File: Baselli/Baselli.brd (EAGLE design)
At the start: 54 x 54 mm, 81 parts, among them J1 FTDI-SER-6-PP, J2 DF12-ELLI-HEADER-TOP, J3 DF12-ELLI-RECEPTABLE-BOTTOM, J4 JTAG_PROG, Q1 8MHz NP, Q2 IRLML2244, SW1 A6H-2101, U1 STM32F051R, U4 LCMXO2-256HC-4SG32, X1 M-BOLT-2, X2 M-BOLT-2, X3 M-BOLT-2, X4 M-BOLT-2, X5 POE-TP-PD-BELFUSE-T568A, Y1 32.768 kHz

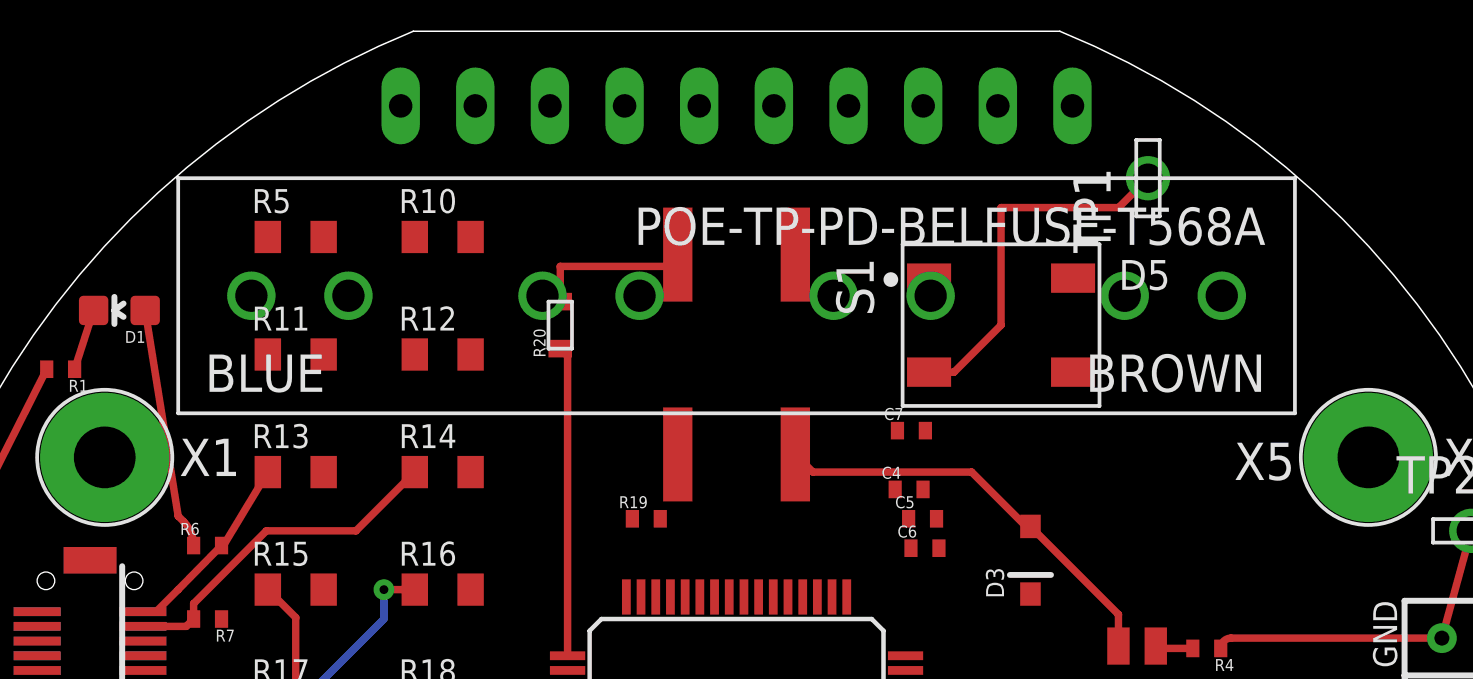
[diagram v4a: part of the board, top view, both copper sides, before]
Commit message: Remove excess punchdown connector from Baselli
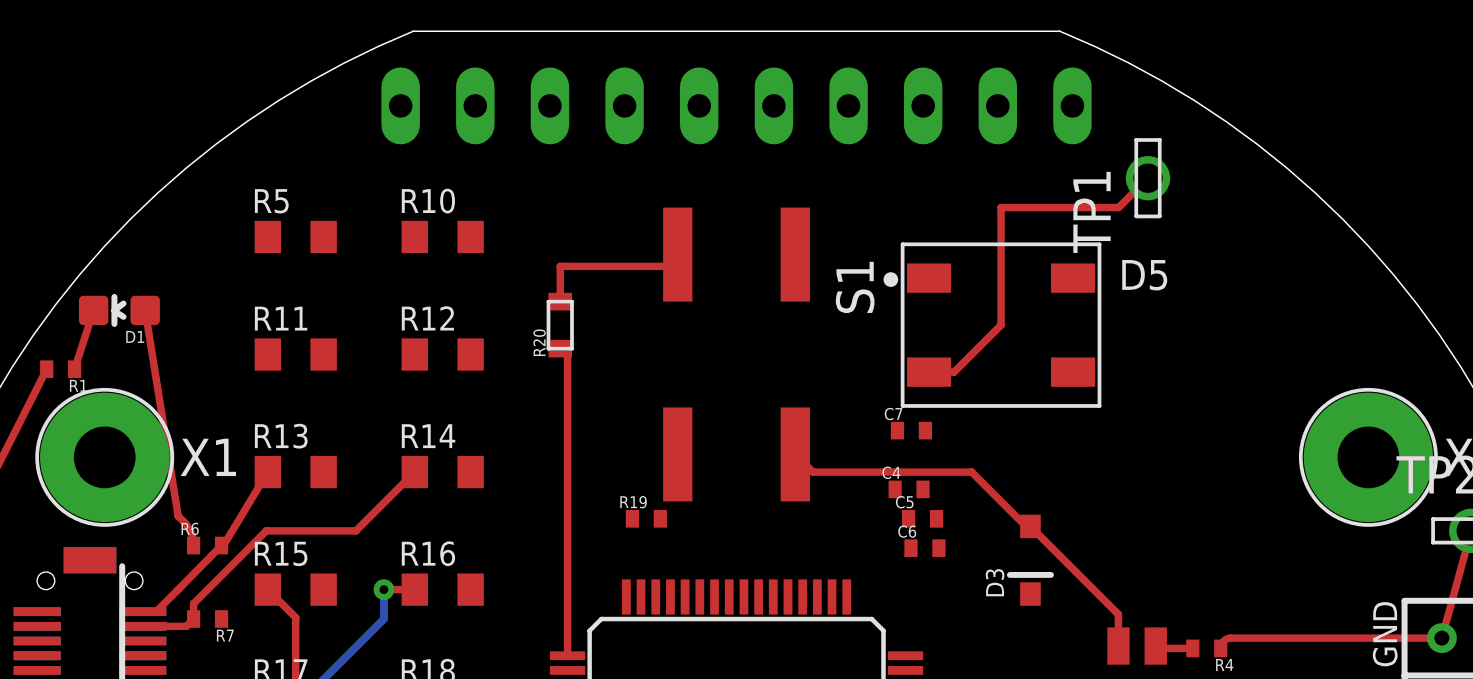
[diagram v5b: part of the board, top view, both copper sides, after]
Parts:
- removed X5: POE-TP-PD-BELFUSE-T568A, ELL-i-Connectors:BELFUSE-SS-51-PD-T568A
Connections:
- removed net POE+: X5.4, X5.5
- removed net POE-: X5.7, X5.8
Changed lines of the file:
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@@
 <layer number="17" name="Pads" color="2" fill="1" visible="yes" active="yes"/>
 <layer number="18" name="Vias" color="2" fill="1" visible="yes" active="yes"/>
-<layer number="19" name="Unrouted" color="6" fill="1" visible="yes" active="yes"/>
+<layer number="19" name="Unrouted" color="6" fill="1" visible="no" active="yes"/>
 <layer number="20" name="Dimension" color="15" fill="1" visible="yes" active="yes"/>
 <layer number="21" name="tPlace" color="7" fill="1" visible="yes" active="yes"/>
@@
 <element name="X4" library="ELL-i-Connectors" package="M2-1" value="M-BOLT-2" x="48.5" y="14.5"/>
 <element name="X3" library="ELL-i-Connectors" package="M2-1" value="M-BOLT-2" x="5.5" y="14.5"/>
-<element name="X5" library="ELL-i-Connectors" package="BELFUSE-SS-51-PD-T568A" value="POE-TP-PD-BELFUSE-T568A" x="27" y="45" rot="R180"/>
 </elements>
 <signals>
@@
 <wire x1="12.1" y1="16" x2="23.25" y2="23.25" width="0" layer="19" extent="1-1"/>
 </signal>
-<signal name="POE+">
-<contactref element="X5" pad="4"/>
-<contactref element="X5" pad="5"/>
-<wire x1="13.792" y1="45" x2="10.49" y2="45" width="0" layer="19" extent="1-1"/>
-</signal>
-<signal name="POE-">
-<contactref element="X5" pad="7"/>
-<contactref element="X5" pad="8"/>
-<wire x1="40.208" y1="45" x2="43.51" y2="45" width="0" layer="19" extent="1-1"/>
-</signal>
 </signals>

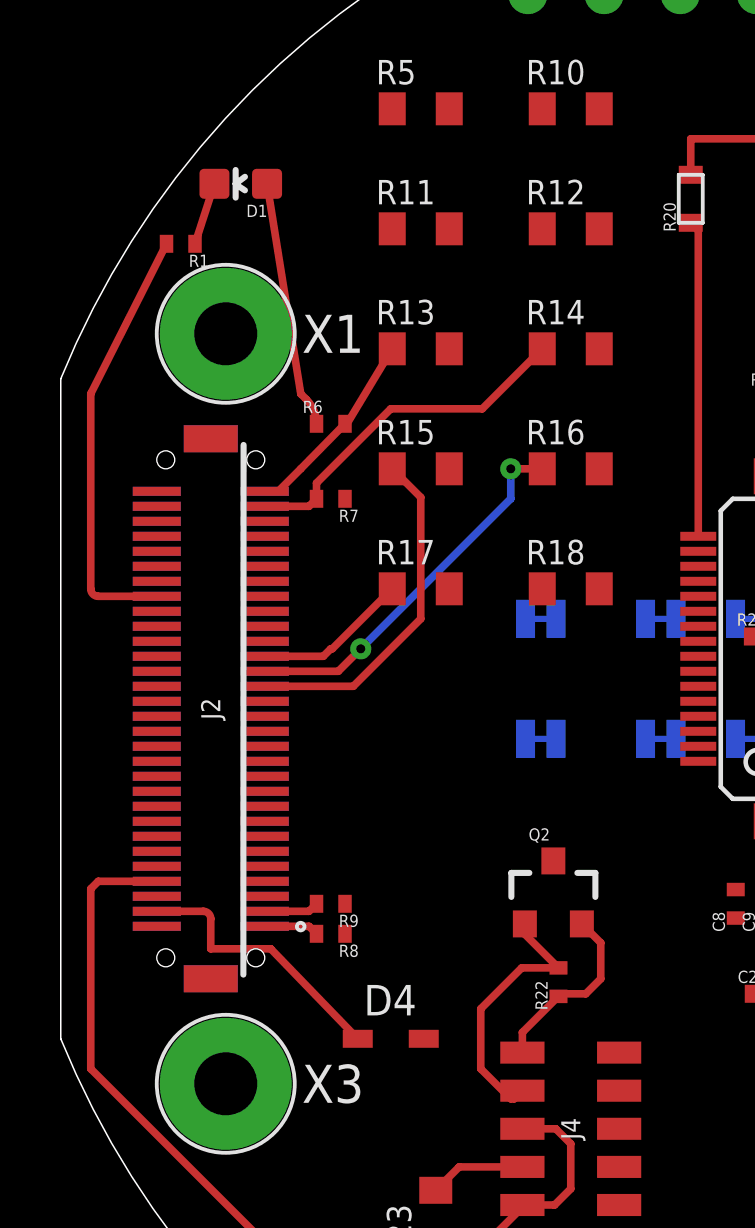
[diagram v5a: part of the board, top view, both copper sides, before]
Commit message: Move Hirose DF12 locations as agreed yesterday
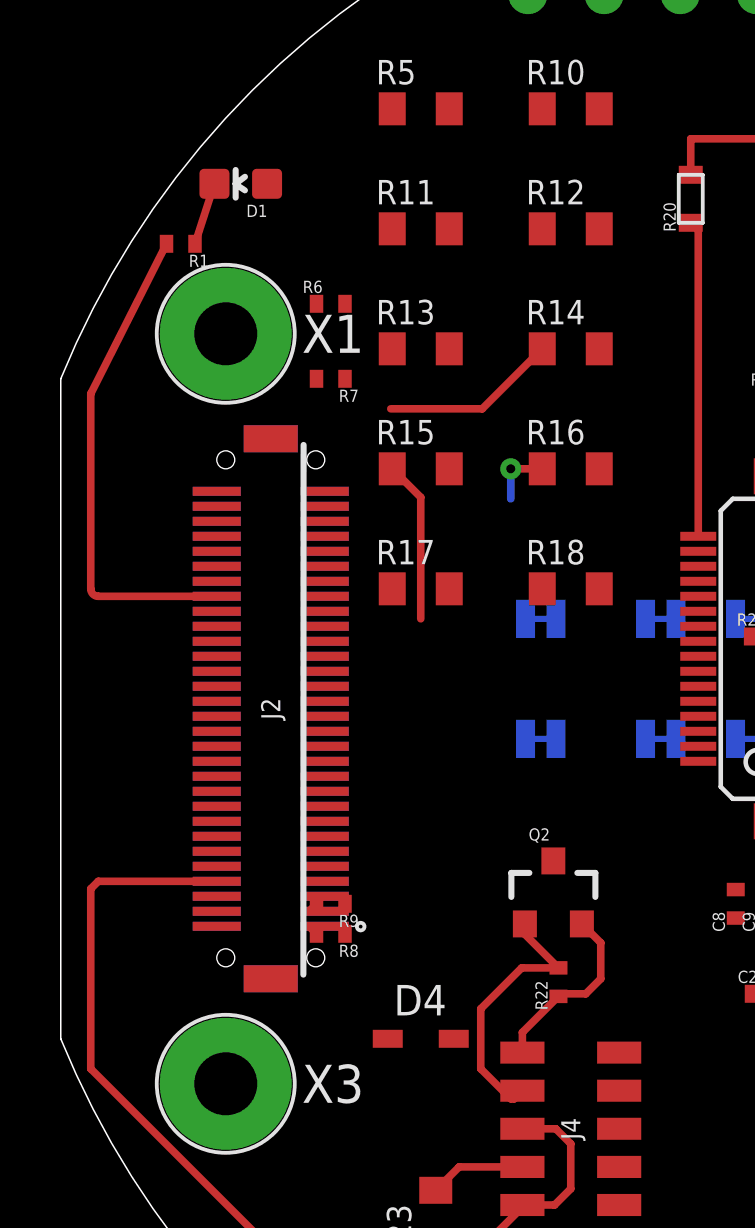
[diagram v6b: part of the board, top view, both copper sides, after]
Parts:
- moved R6 4.00 mm to (9.00, 40.5)
- moved R7 4.00 mm to (9.00, 38.0)
- moved J2 2.00 mm to (7.00, 27.0)
- moved J3 2.00 mm to (7.00, 27.0)
- moved D4 1.00 mm to (12.0, 16.0)
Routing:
- net E1: track 12.6 -> 2.05 mm, vias 2 -> 1
- net VBATT: track 9.08 -> 0.45 mm
- net +3V3: track 51.5 -> 43.3 mm
- net E13: track 6.62 -> 0.00 mm
- net E0: track 11.5 -> 5.39 mm
- net E12: track 11.7 -> 5.88 mm
- net E2: track 5.18 -> 0.00 mm
- net GNDI: track 39.9 -> 41.9 mm
- net +5V: track 56.2 -> 58.2 mm
- net A5: track 1.83 -> 0.88 mm
- net A4: track 1.83 -> 0.88 mm

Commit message: Preliminary work on Baselli
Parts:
- added C12: 100nF, ELL-i-Passives:C0402
- added C13: 1uF, ELL-i-Passives:C0402
- D3: value BAT60J -> DIODE-SCHOTTKY-BAT60J; device ell-i:SOD323_DIODE -> SparkFun-DiscreteSemi:SOD-323
- R10, R11, R12, R13, R14, R15, R16, R17, R18, R23, R5: device ELL-i-Passives:R0805 -> ELL-i-Passives:R0603
- moved R20 38.8 mm to (16.5, 5.50), turned to 0 degrees
- moved C4 26.1 mm to (29.5, 12.5), turned to 270 degrees
- moved C5 25.4 mm to (28.5, 12.5), turned to 90 degrees
- moved R5 23.0 mm to (13.0, 24.0)
- moved SJ6 19.2 mm to (29.0, 44.5)
- moved R11 17.6 mm to (16.5, 26.0)
- moved R12 17.5 mm to (13.0, 26.0)
- moved SJ5 17.1 mm to (25.0, 44.5)
- moved R21 15.9 mm to (22.4, 13.5), turned to 270 degrees
- moved SJ11 12.5 mm to (26.5, 18.0)
- moved SJ15 12.5 mm to (19.5, 18.0), turned to 180 degrees
- moved SJ9 12.5 mm to (29.5, 18.0)
- moved SJ13 12.3 mm to (22.5, 18.0), turned to 180 degrees
- moved SJ7 12.2 mm to (32.0, 18.0)
- moved SJ10 11.5 mm to (29.5, 15.0)
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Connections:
- net +3V3: now also C12.1, C13.1, D3.C; no longer D3.1
- net GNDI: now also C12.2, C13.2
- net NRES: now also D3.A; no longer D3.2
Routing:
- net +5V: track 58.2 -> 3.59 mm
- net GNDI: track 41.9 -> 0.00 mm
- net D3: track 0.00 -> 35.0 mm, vias 0 -> 2
- net E14: track 0.00 -> 34.7 mm, vias 0 -> 1
- net D12: track 0.00 -> 31.8 mm
- net NRES: track 14.3 -> 46.0 mm, vias 0 -> 2
- net E16: track 0.00 -> 31.6 mm, vias 0 -> 1
- net E17: track 0.00 -> 30.2 mm, vias 0 -> 1
- net E15: track 0.00 -> 28.8 mm, vias 0 -> 1
- net PF7: track 0.00 -> 25.8 mm, vias 0 -> 4
- net SN: track 0.00 -> 24.0 mm
- net E10: track 0.00 -> 23.6 mm, vias 0 -> 1
- net PF6: track 0.00 -> 23.4 mm, vias 0 -> 2
- net E11: track 0.00 -> 23.2 mm, vias 0 -> 1
- net SWDIO: track 0.00 -> 18.9 mm, vias 0 -> 2
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
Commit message: More preliminary work on Baselli
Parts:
- moved X2 50.2 mm to (5.50, 13.5)
- moved X3 50.2 mm to (48.5, 40.5)
- moved R1 10.2 mm to (14.0, 44.5), turned to 90 degrees
- moved D1 8.54 mm to (14.0, 41.5), turned to 0 degrees
- moved FB2 2.58 mm to (27.4, 21.5), turned to 180 degrees
- moved D3 2.50 mm to (37.5, 36.0)
- moved SJ3 2.06 mm to (30.0, 6.00)
- moved SJ4 2.06 mm to (35.0, 6.00)
- moved SJ1 2.00 mm to (19.5, 6.00)
- moved SJ2 2.00 mm to (24.5, 6.00)
- moved SJ10 1.00 mm to (29.5, 14.0)
- moved SJ11 1.00 mm to (26.5, 17.0)
- moved SJ12 1.00 mm to (26.5, 14.0)
- moved SJ13 1.00 mm to (22.5, 17.0)
- moved SJ14 1.00 mm to (22.5, 14.0)
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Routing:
- net +3V3: track 52.1 -> 5.40 mm
- net PA7: track 0.00 -> 43.0 mm
- net CSSPIN: track 0.00 -> 36.0 mm, vias 0 -> 2
- net JTDI: track 9.97 -> 45.5 mm, vias 0 -> 4
- net SWDIO: track 18.9 -> 48.6 mm, vias 2 -> 3
- net PROGRAMN: track 0.00 -> 29.1 mm, vias 0 -> 2
- net SWCLK: track 18.8 -> 46.8 mm, vias 0 -> 2
- net D5: track 0.00 -> 27.7 mm, vias 0 -> 3
- net MCO: track 0.00 -> 26.8 mm, vias 0 -> 2
- net PF5: track 0.00 -> 22.8 mm, vias 0 -> 2
- net D10: track 15.5 -> 37.2 mm, vias 0 -> 3
- net D13: track 0.00 -> 19.0 mm, vias 0 -> 2
- net PB11: track 0.00 -> 18.9 mm, vias 0 -> 2
- net D11: track 0.00 -> 18.2 mm, vias 0 -> 4
- net PF4: track 0.00 -> 17.4 mm, vias 0 -> 2
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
